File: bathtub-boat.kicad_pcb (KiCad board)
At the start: 2 copper layers, 0.9 x 15 mm, 3 parts, among them U1 esp-01m, U2 tp4056, U3 LM4950TA

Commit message: Add components
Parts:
- added BT3: Battery_Cell, Connector_JST:JST_PH_B2B-PH-K_1x02_P2.00mm_Vertical, F.Cu at (150.0, 38.0)
- added J1: I2C, Connector_JST:JST_SH_SM04B-SRSS-TB_1x04-1MP_P1.00mm_Horizontal, B.Cu at (111.0, 58.0)
- added J2: SPI, Connector_PinHeader_2.54mm:PinHeader_1x06_P2.54mm_Vertical, F.Cu at (128.3, 39.0)
- added SW1: MODE, Button_Switch_SMD:SW_Push_1P1T_NO_Vertical_Wuerth_434133025816, B.Cu at (132.0, 54.0)
- added SW2: RESET, Button_Switch_SMD:SW_Push_1P1T_NO_Vertical_Wuerth_434133025816, B.Cu at (115.0, 45.0)
- added SW4: A, Button_Switch_SMD:SW_Push_1P1T_NO_Vertical_Wuerth_434133025816, B.Cu at (119.0, 68.0)
- added U4: DS18B20, Package_TO_SOT_THT:TO-92_Inline_Wide, F.Cu at (124.0, 67.0)
- added U5: TTL, Connector_PinHeader_2.54mm:PinHeader_1x04_P2.54mm_Vertical, F.Cu at (138.0, 45.0)
- U1: moved to B.Cu
- U3: value LM4950TA -> UA78M33_TO252; footprint Package_TO_SOT_THT:TO-220-5_P3.4x3.7mm_StaggerOdd_Lead3.8mm_Vertical -> Package_TO_SOT_SMD:TO-252-2; moved to B.Cu
- moved U1 45.1 mm to (121.0, 51.0), turned to 180 degrees
- moved U3 41.9 mm to (134.0, 64.0)
- moved U2 17.1 mm to (142.8, 67.6), turned to 90 degrees
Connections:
- U1 pad 1: unconnected-(U1-Pad1) -> GND
- U1 pad 10: unconnected-(U1-Pad10) -> I2C_SDA
- U1 pad 11: unconnected-(U1-Pad11) -> TEMP
- U1 pad 12: unconnected-(U1-Pad12) -> Neopixel
- U1 pad 13: unconnected-(U1-Pad13) -> I2C_SCL
- U1 pad 14: unconnected-(U1-Pad14) -> SPI_MISO
- U1 pad 15: unconnected-(U1-Pad15) -> SPI_CLK
- U1 pad 17: unconnected-(U1-Pad17) -> Net-(U1-Pad17)
- U1 pad 18: unconnected-(U1-Pad18) -> Net-(U1-Pad17)
- U1 pad 2: unconnected-(U1-Pad2) -> +3V3
- U1 pad 3: unconnected-(U1-Pad3) -> TX
- U1 pad 4: unconnected-(U1-Pad4) -> RX
- U1 pad 5: unconnected-(U1-Pad5) -> SPI_MOSI
- U1 pad 6: unconnected-(U1-Pad6) -> SPI_CS
- U1 pad 7: unconnected-(U1-Pad7) -> BUTTON-A
- U1 pad 8: unconnected-(U1-Pad8) -> Net-(SW1-Pad2)
- U1 pad 9: unconnected-(U1-Pad9) -> +3V3
- U2 pad 1: unconnected-(U2-Pad1) -> VBUS
- U2 pad 2: unconnected-(U2-Pad2) -> GND
- U2 pad 3: unconnected-(U2-Pad3) -> +5V
- U2 pad 4: unconnected-(U2-Pad4) -> GND
- U3 pad 1: unconnected-(U3-Pad1) -> +5V
- U3 pad 2: unconnected-(U3-Pad2) -> GND
- U3 pad 3: unconnected-(U3-Pad3) -> +3V3
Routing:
- net +3V3: track 0.00 -> 81.6 mm, vias 0 -> 2
- net SPI_CS: track 0.00 -> 47.0 mm, vias 0 -> 4
- net SPI_MISO: track 0.00 -> 37.9 mm
- net +5V: track 0.00 -> 37.8 mm
- net BUTTON-A: track 0.00 -> 28.5 mm, vias 0 -> 2
- net SPI_CLK: track 0.00 -> 24.1 mm
- net GND: track 0.00 -> 23.4 mm, vias 0 -> 4
- net TEMP: track 0.00 -> 19.7 mm, vias 0 -> 2
- net SPI_MOSI: track 0.00 -> 18.6 mm, vias 0 -> 2
- net TX: track 0.00 -> 17.9 mm
- net RX: track 0.00 -> 15.5 mm
- net Net-(U1-Pad17): track 0.00 -> 8.59 mm
- net Net-(SW1-Pad2): track 0.00 -> 8.26 mm
- net I2C_SCL: track 0.00 -> 8.25 mm
- net Net-(BT1-Pad2): track 0.00 -> 6.49 mm
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- added copper zone on B.Cu, net GND
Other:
- board size 0.9 x 15 mm -> 55 x 38 mm

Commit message: Prepare for milling
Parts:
- U2: value tp4056 -> TP4056
- moved U2 15.0 mm to (150.2, 54.5)
- moved U3 3.01 mm to (136.2, 62.0), turned to 90 degrees
- moved SW4 1.79 mm to (117.4, 67.2)
- moved J2 1.40 mm to (128.3, 37.6)
- moved BT3 0.76 mm to (149.3, 37.7)
- moved U5 0.76 mm to (137.8, 44.3)
- moved SW1 0.34 mm to (131.8, 54.2)
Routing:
- net GND: track 23.4 -> 14.7 mm, vias 4 -> 2
- net +3V3: track 81.6 -> 86.2 mm
- net SPI_CS: track 47.0 -> 42.7 mm, vias 4 -> 2
- net +5V: track 37.8 -> 33.9 mm
- net SPI_MISO: track 37.9 -> 34.4 mm, vias 0 -> 2
- net Neopixel: track 0.00 -> 3.41 mm, vias 0 -> 1
- net Net-(SW1-Pad2): track 8.26 -> 11.2 mm
- net TX: track 17.9 -> 15.4 mm
- net TEMP: track 19.7 -> 18.2 mm
- net BUTTON-A: track 28.5 -> 29.5 mm
- net I2C_SCL: track 8.25 -> 9.21 mm
- net SPI_MOSI: track 18.6 -> 19.6 mm
- net RX: track 15.5 -> 15.0 mm
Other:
- board size 55 x 38 mm -> 52.7 x 37.6 mm

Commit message: Closer layout
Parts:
- moved SW4 15.2 mm to (132.0, 63.0), turned to 90 degrees
- moved U3 14.1 mm to (143.6, 50.0), turned to 180 degrees
- moved BT3 6.48 mm to (142.8, 37.7)
- moved U2 6.48 mm to (143.7, 54.5)
- moved U5 4.98 mm to (133.0, 43.0)
- moved U4 1.93 mm to (124.1, 65.1)
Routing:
- net +5V: track 33.9 -> 14.8 mm
- net +3V3: track 86.2 -> 76.8 mm
- net BUTTON-A: track 29.5 -> 20.2 mm
- net RX: track 15.0 -> 10.6 mm
- net TX: track 15.4 -> 11.1 mm
- net SPI_CS: track 42.7 -> 39.0 mm
- net Neopixel: track 3.41 -> 4.65 mm
- net TEMP: track 18.2 -> 17.2 mm
- net GND: track 14.7 -> 13.8 mm
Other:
- board size 52.7 x 37.6 mm -> 44.7 x 33.2 mm

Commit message: Add readme and fix 3d model of lipo charger
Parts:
- U4: moved to B.Cu
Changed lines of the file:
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@@
   (net 19 "SPI_CLK")
   (net 20 "Neopixel")
-  (footprint "Package_TO_SOT_THT:TO-92_Inline_Wide" (layer "F.Cu")
-    (at 124.052171 65.072563 90)
-    (descr "TO-92 leads in-line, wide, drill 0.75mm (see NXP sot054_po.pdf)")
-    (tags "to-92 sc-43 sc-43a sot54 PA33 transistor")
-    (property "Sheetfile" "bathtub-boat.kicad_sch")
-    (property "Sheetname" "")
-    (attr through_hole)
-    (fp_text reference "U4" (at 2.54 -3.56 90) (layer "F.SilkS")
-      (effects (font (size 1 1) (thickness 0.15)))
-    )
-    (fp_text value "DS18B20" (at 2.54 2.79 90) (layer "F.Fab")
-      (effects (font (size 1 1) (thickness 0.15)))
-    )
-    (fp_text user "${REFERENCE}" (at 2.54 0 90) (layer "F.Fab")
-      (effects (font (size 1 1) (thickness 0.15)))
-    )
-    (fp_line (start 0.74 1.85) (end 4.34 1.85) (layer "F.SilkS") (width 0.12))
-    (fp_arc (start 4.864184 1.122795) (mid 4.633903 1.509328) (end 4.34 1.85) (layer "F.SilkS") (width 0.12))
-    (fp_arc (start 2.54 -2.6) (mid 3.936979 -2.192818) (end 4.8964 -1.098807) (layer "F.SilkS") (width 0.12))
-    (fp_arc (start 0.1836 -1.098807) (mid 1.143021 -2.192817) (end 2.54 -2.6) (layer "F.SilkS") (width 0.12))
-    (fp_arc (start 0.74 1.85) (mid 0.446097 1.509328) (end 0.215816 1.122795) (layer "F.SilkS") (width 0.12))
-    (fp_line (start 6.09 2.01) (end -1.01 2.01) (layer "F.CrtYd") (width 0.05))
-    (fp_line (start 6.09 2.01) (end 6.09 -2.73) (layer "F.CrtYd") (width 0.05))
-    (fp_line (start -1.01 -2.73) (end -1.01 2.01) (layer "F.CrtYd") (width 0.05))
-    (fp_line (start -1.01 -2.73) (end 6.09 -2.73) (layer "F.CrtYd") (width 0.05))
-    (fp_line (start 0.8 1.75) (end 4.3 1.75) (layer "F.Fab") (width 0.1))
-    (fp_arc (start 2.54 -2.48) (mid 4.831221 -0.949055) (end 4.293625 1.753625) (layer "F.Fab") (width 0.1))
-    (fp_arc (start 0.786375 1.753625) (mid 0.248779 -0.949055) (end 2.54 -2.48) (layer "F.Fab") (width 0.1))
-    (pad "1" thru_hole oval (at 0 0 180) (size 2.5 1.7) (drill 1) (layers *.Cu *.Mask)
-      (net 1 "GND") (pinfunction "GND") (pintype "power_in"))
-    (pad "2" thru_hole oval (at 2.54 0 180) (size 2.5 1.7) (drill 1) (layers *.Cu *.Mask)
-      (net 9 "TEMP") (pinfunction "DQ") (pintype "bidirectional"))
-    (pad "3" thru_hole oval (at 5.08 0 180) (size 2.5 1.7) (drill 1) (layers *.Cu *.Mask)
-      (net 4 "+3V3") (pinfunction "VDD") (pintype "power_in"))
-    (model "${KICAD6_3DMODEL_DIR}/Package_TO_SOT_THT.3dshapes/TO-92_Inline_Wide.wrl"
-      (offset (xyz 0 0 0))
-      (scale (xyz 1 1 1))
-      (rotate (xyz 0 0 0))
-    )
-  )
   (footprint "Connector_JST:JST_PH_B2B-PH-K_1x02_P2.00mm_Vertical" (layer "F.Cu")
     (at 142.821086 37.7)
@@
       (net 10 "Net-(BT1-Pad2)") (pinfunction "B-") (pintype "power_in"))
     (model "${KIPRJMOD}/lib/tp4056/tp4056.step"
-      (offset (xyz 13 -9 0))
+      (offset (xyz 0 0 0))
       (scale (xyz 1 1 1))
       (rotate (xyz 0 0 0))
@@
       (offset (xyz 0 0 0))
       (scale (xyz 1 1 1))
+      (rotate (xyz 0 0 0))
+    )
+  )
+  (footprint "Package_TO_SOT_THT:TO-92_Inline_Wide" (layer "B.Cu")
+    (at 124.052171 65.072563 90)
+    (descr "TO-92 leads in-line, wide, drill 0.75mm (see NXP sot054_po.pdf)")
+    (tags "to-92 sc-43 sc-43a sot54 PA33 transistor")
+    (property "Sheetfile" "bathtub-boat.kicad_sch")
+    (property "Sheetname" "")
+    (attr through_hole)
+    (fp_text reference "U4" (at 2.54 3.56 90) (layer "B.SilkS")
+      (effects (font (size 1 1) (thickness 0.15)) (justify mirror))
+    )
+    (fp_text value "DS18B20" (at 2.54 -2.79 90) (layer "B.Fab")
+      (effects (font (size 1 1) (thickness 0.15)) (justify mirror))
+    )
+    (fp_text user "${REFERENCE}" (at 2.54 0 90) (layer "B.Fab")
+      (effects (font (size 1 1) (thickness 0.15)) (justify mirror))
+    )
+    (fp_line (start 0.74 -1.85) (end 4.34 -1.85) (layer "B.SilkS") (width 0.12))
+    (fp_arc (start 4.34 -1.85) (mid 4.633903 -1.509328) (end 4.864184 -1.122795) (layer "B.SilkS") (width 0.12))
+    (fp_arc (start 4.8964 1.098807) (mid 3.936979 2.192817) (end 2.54 2.6) (layer "B.SilkS") (width 0.12))
+    (fp_arc (start 2.54 2.6) (mid 1.143021 2.192818) (end 0.1836 1.098807) (layer "B.SilkS") (width 0.12))
+    (fp_arc (start 0.215816 -1.122795) (mid 0.446097 -1.509328) (end 0.74 -1.85) (layer "B.SilkS") (width 0.12))
+    (fp_line (start 6.09 -2.01) (end -1.01 -2.01) (layer "B.CrtYd") (width 0.05))
+    (fp_line (start 6.09 -2.01) (end 6.09 2.73) (layer "B.CrtYd") (width 0.05))
+    (fp_line (start -1.01 2.73) (end -1.01 -2.01) (layer "B.CrtYd") (width 0.05))
+    (fp_line (start -1.01 2.73) (end 6.09 2.73) (layer "B.CrtYd") (width 0.05))
+    (fp_line (start 0.8 -1.75) (end 4.3 -1.75) (layer "B.Fab") (width 0.1))
+    (fp_arc (start 4.293625 -1.753625) (mid 4.831221 0.949055) (end 2.54 2.48) (layer "B.Fab") (width 0.1))
+    (fp_arc (start 2.54 2.48) (mid 0.248779 0.949055) (end 0.786375 -1.753625) (layer "B.Fab") (width 0.1))
+    (pad "1" thru_hole oval (at 0 0) (size 2.5 1.7) (drill 1) (layers *.Cu *.Mask)
+      (net 1 "GND") (pinfunction "GND") (pintype "power_in"))
+    (pad "2" thru_hole oval (at 2.54 0) (size 2.5 1.7) (drill 1) (layers *.Cu *.Mask)
+      (net 9 "TEMP") (pinfunction "DQ") (pintype "bidirectional"))
+    (pad "3" thru_hole oval (at 5.08 0) (size 2.5 1.7) (drill 1) (layers *.Cu *.Mask)
+      (net 4 "+3V3") (pinfunction "VDD") (pintype "power_in"))
+    (model "${KICAD6_3DMODEL_DIR}/Package_TO_SOT_THT.3dshapes/TO-92_Inline_Wide.wrl"
+      (offset (xyz 0 0 0))
+      (scale (xyz 1 1 1))

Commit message: Prepare the pcb for next iteration
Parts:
- added BT1: Battery_Cell, Connector_JST:JST_GH_BM02B-GHS-TBT_1x02-1MP_P1.25mm_Vertical, F.Cu at (143.5, 29.5)
- U2: value TP4056 -> tp4056
- moved SW4 1.15 mm to (132.1, 64.2)
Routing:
- net Net-(SW1-Pad2): track 11.5 -> 7.43 mm
- net +3V3: track 76.8 -> 75.3 mm
- net BUTTON-A: track 20.2 -> 21.0 mm
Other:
- board text added: "BTB v1.1-beta 22.1.24"
- board text added: "TODO: - Add a battery switch - THT push button on the top side"

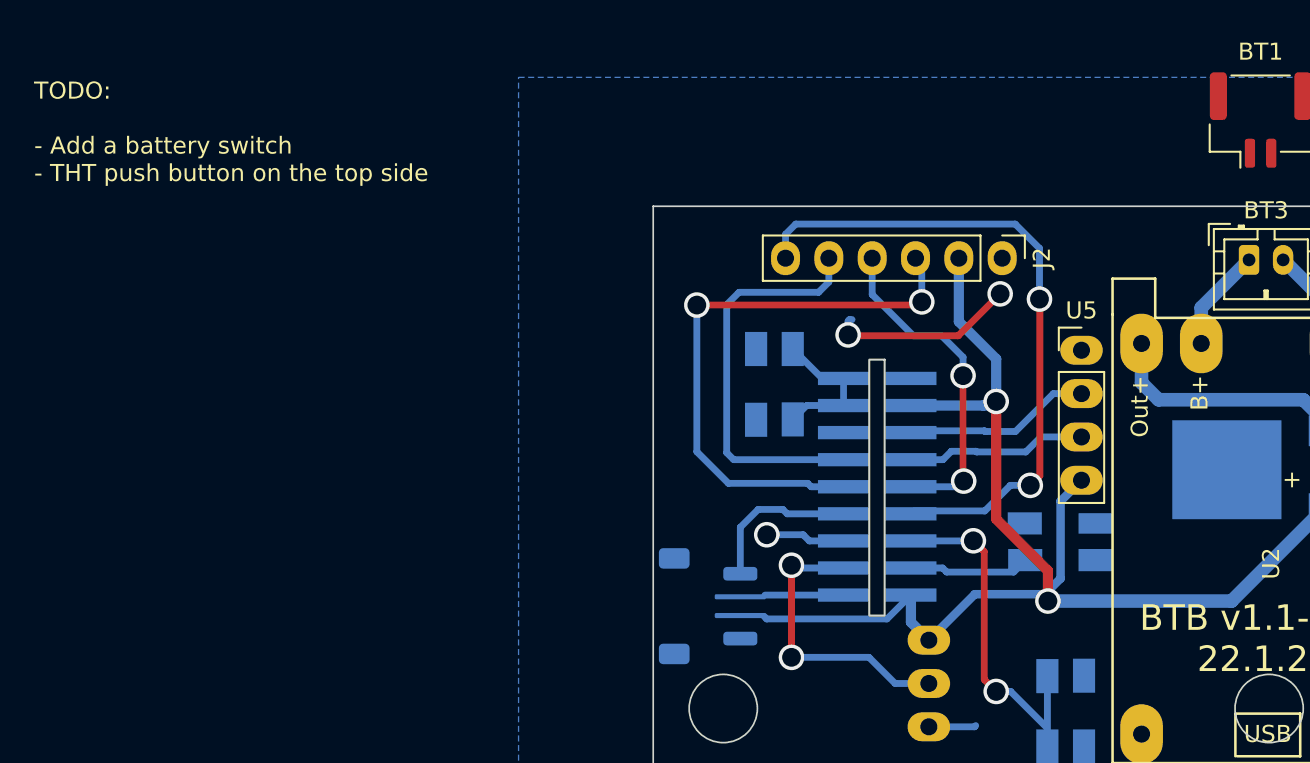
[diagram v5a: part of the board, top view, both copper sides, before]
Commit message: Minor changes to board, reflect tp4056 connections, todos for upcoming version
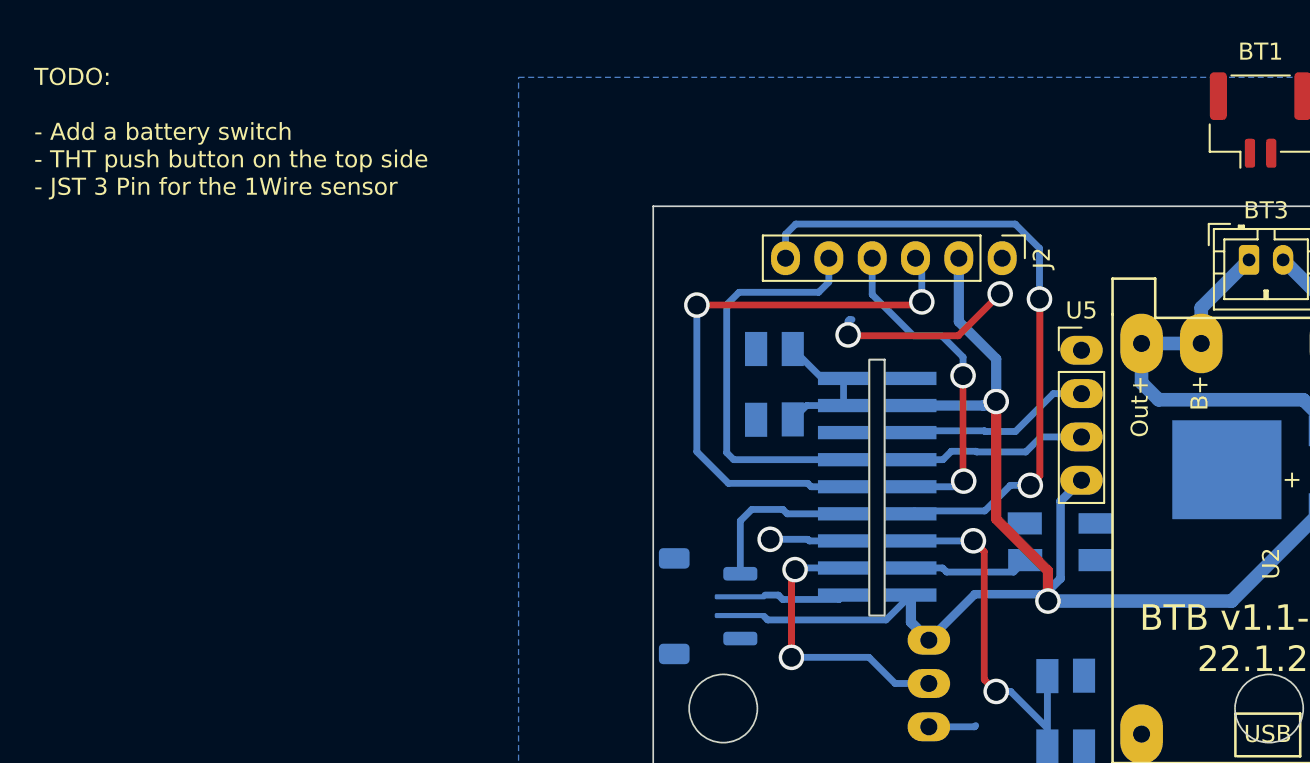
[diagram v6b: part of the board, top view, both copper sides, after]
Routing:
- net +5V: track 14.8 -> 24.3 mm
- net Net-(BT1-Pad1): track 6.06 -> 0.00 mm
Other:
- board text added: "TODO: - Add a battery switch - THT push button on the top side - JST 3 Pin for the 1Wire sensor"
- board text removed: "TODO: - Add a battery switch - THT push button on the top side"

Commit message: New PCB version 2.0
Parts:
- removed BT1: Battery_Cell, Connector_JST:JST_GH_BM02B-GHS-TBT_1x02-1MP_P1.25mm_Vertical
- removed U4: DS18B20, Package_TO_SOT_THT:TO-92_Inline_Wide
- added D1: WS2812B, LED_THT:LED_D5.0mm-4_RGB_Wide_Pins, F.Cu at (136.0, 79.8)
- added H1: MountingHole, MountingHole:MountingHole_3.2mm_M3, F.Cu at (104.0, 70.0)
- added H2: MountingHole, MountingHole:MountingHole_3.2mm_M3, F.Cu at (155.0, 70.0)
- added H3: MountingHole, MountingHole:MountingHole_3.2mm_M3, F.Cu at (104.0, 96.0)
- added J3: I2C, Connector_PinHeader_2.54mm:PinHeader_1x04_P2.54mm_Vertical, F.Cu at (128.8, 91.4)
- added J4: DS18B20, Connector_JST:JST_XH_B3B-XH-A_1x03_P2.50mm_Vertical, F.Cu at (137.9, 95.7)
- added SW3: POWER, Connector_PinHeader_2.54mm:PinHeader_1x03_P2.54mm_Vertical, F.Cu at (137.0, 69.6)
- added TP1: ADC, TestPoint:TestPoint_THTPad_2.0x2.0mm_Drill1.0mm, B.Cu at (112.2, 86.0)
- added U6: magnetic-charger, magnetic-charger:magnetic-charger, F.Cu at (113.5, 93.8)
- added kibuzzard-65B79508: G***, kibuzzard-65B79508, F.Cu at (125.0, 94.4)
- added kibuzzard-65B79597: G***, kibuzzard-65B79597, F.Cu at (101.2, 88.3)
- added kibuzzard-65B7959E: G***, kibuzzard-65B7959E, F.Cu at (129.6, 76.4)
- added kibuzzard-65B795B9: G***, kibuzzard-65B795B9, F.Cu at (146.8, 67.2)
- added kibuzzard-65B795B9: G***, kibuzzard-65B795B9, F.Cu at (127.4, 80.8)
- added kibuzzard-65B795B9: G***, kibuzzard-65B795B9, F.Cu at (136.0, 78.0)
- added kibuzzard-65B7965E: G***, kibuzzard-65B7965E, F.Cu at (101.2, 79.8)
- added kibuzzard-65B796EF: G***, kibuzzard-65B796EF, F.Cu at (124.6, 96.6)
- added kibuzzard-65B796FD: G***, kibuzzard-65B796FD, F.Cu at (117.0, 72.4)
- added kibuzzard-65B8C3A2: G***, kibuzzard-65B8C3A2, F.Cu at (117.4, 67.3)
- added kibuzzard-65B8C65E: G***, kibuzzard-65B8C65E, F.Cu at (135.6, 99.0)
- added kibuzzard-65B8C757: G***, kibuzzard-65B8C757, F.Cu at (129.5, 71.1)
- SW1, SW2, SW4: footprint Button_Switch_SMD:SW_Push_1P1T_NO_Vertical_Wuerth_434133025816 -> pts636:pts636; moved to F.Cu
- moved U5 49.9 mm to (103.8, 83.4), turned to 180 degrees
- moved SW2 41.9 mm to (103.8, 85.4)
- moved J1 41.1 mm to (124.4, 96.8), turned to 180 degrees
- moved J2 36.8 mm to (111.0, 70.0), turned to 90 degrees
- moved U3 34.9 mm to (148.0, 84.6)
- moved U2 33.1 mm to (150.0, 87.0)
- moved BT3 32.6 mm to (147.0, 70.0)
- moved U1 32.0 mm to (121.0, 83.0), turned to -90 degrees
- moved SW1 25.2 mm to (132.2, 79.4), turned to 90 degrees
- moved SW4 4.47 mm to (132.7, 68.6), turned to 180 degrees
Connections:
- net BUTTON-A renamed Net-(SW4-Pad2)
- BT3 pad 1: Net-(BT1-Pad1) -> /BAT+
- BT3 pad 2: Net-(BT1-Pad2) -> /BAT-
- U1 pad 10: I2C_SDA -> Temp
- U1 pad 11: TEMP -> Neopixel
- U1 pad 12: Neopixel -> I2C_SDA
- U1 pad 16: unconnected-(U1-Pad16) -> Net-(TP1-Pad1)
- U2 pad 3: +5V -> /BAT+
- U2 pad 6: Net-(BT1-Pad2) -> GND
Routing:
- net VBUS: track 0.00 -> 36.1 mm, vias 0 -> 2
- net +3V3: track 75.4 -> 106.8 mm, vias 2 -> 6
- net SPI_CS: track 39.0 -> 11.5 mm, vias 2 -> 0
- net SPI_CLK: track 23.6 -> 48.5 mm, vias 0 -> 2
- net TEMP: track 16.8 -> 0.00 mm, vias 2 -> 0
- net Neopixel: track 4.34 -> 21.0 mm, vias 1 -> 2
- net Temp: track 0.00 -> 14.9 mm
- net /BAT+: track 0.00 -> 14.4 mm
- net GND: track 13.8 -> 3.34 mm, vias 2 -> 0
- net Net-(SW2-Pad2): track 8.59 -> 18.9 mm
- net RX: track 10.6 -> 20.4 mm
- net Net-(SW1-Pad2): track 7.43 -> 16.3 mm
- net Net-(TP1-Pad1): track 0.00 -> 8.82 mm
- net /BAT-: track 0.00 -> 8.31 mm
- net Net-(SW4-Pad2): track 21.0 -> 13.3 mm, vias 2 -> 0
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- added copper zone on B.Cu, net +3V3
- added copper zone on B.Cu, net I2C_SDA
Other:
- board size 44.7 x 33.2 mm -> 59.3 x 34 mm
- board text added: "Bathtubboat v2.0 29.01.2024"
- board text removed: "BTB v1.1-beta 22.1.24"
- board text removed: "TODO: - Add a battery switch - THT push button on the top side - JST 3 Pin for the 1Wire sensor"

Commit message: Add power switch
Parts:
- added kibuzzard-65B98079: G***, kibuzzard-65B98079, F.Cu at (142.2, 72.4)
- added kibuzzard-65B98083: G***, kibuzzard-65B98083, F.Cu at (137.2, 72.4)
- SW3: footprint Connector_PinHeader_2.54mm:PinHeader_1x03_P2.54mm_Vertical -> as12ap:as12ap
- moved U2 0.43 mm to (150.4, 87.2)
- moved SW3 0.08 mm to (137.0, 69.5)
